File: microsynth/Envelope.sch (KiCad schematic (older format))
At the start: 42 parts, among them Q3 BC548, SW18-ENV-TO-VCF1 SW_SPDT, SW19-ENV-TO-VCO1 SW_SPDT, SW20-ENV-TO-KEYB1 SW_SPDT, SW7 SW_SPDT, SW8 SUSTAIN, SW9 TRIGGER, U10 LM741, U3 4011, U4 4016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

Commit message: Clean up repo
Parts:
- U5: symbol Amplifier_Operational:LF347 -> microsynth-rescue:LF347-Amplifier_Operational
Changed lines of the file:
@@
 $EndComp
 $Comp
-L Amplifier_Operational:LF347 U?
+L microsynth-rescue:LF347-Amplifier_Operational U?
 U 2 1 5E8FB113
 P 10250 3650
 AR Path="/5E8C1704/5E8FB113" Ref="U?"  Part="2"
 AR Path="/5E5B9865/5E8FB113" Ref="U5"  Part="2"
+AR Path="/5E8FB113" Ref="U5"  Part="2"
 F 0 "U5" H 10250 4050 50  0000 C CNN
 F 1 "LF347" H 10250 3950 50  0000 C CNN

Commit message: Replace dodgy parts 1458, 4136 & LF351s
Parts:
- removed U5: LF347, Package_DIP:DIP-14_W7.62mm_LongPads, symbol microsynth-rescue:LF347-Amplifier_Operational
- added U5: LF347, Package_DIP:DIP-14_W7.62mm_LongPads, symbol pe_microsynth:LF347
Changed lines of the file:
@@
-$EndComp
-$Comp
-L microsynth-rescue:LF347-Amplifier_Operational U?
-U 2 1 5E8FB113
-P 10250 3650
-AR Path="/5E8C1704/5E8FB113" Ref="U?"  Part="2"
-AR Path="/5E5B9865/5E8FB113" Ref="U5"  Part="2"
-AR Path="/5E8FB113" Ref="U5"  Part="2"
-F 0 "U5" H 10250 4050 50  0000 C CNN
-F 1 "LF347" H 10250 3950 50  0000 C CNN
-F 2 "Package_DIP:DIP-14_W7.62mm_LongPads" H 10200 3750 50  0001 C CNN
-F 3 "https://www.ti.com/lit/ds/symlink/lf147.pdf" H 10300 3850 50  0001 C CNN
-	2    10250 3650
-	1    0    0    -1
 $EndComp
 $Comp
@@
 	1    0    0    1
 $EndComp
+$Comp
+L pe_microsynth:LF347 U?
+U 2 1 5EBDD19A
+P 10250 3650
+AR Path="/5E8C1704/5EBDD19A" Ref="U?"  Part="2"
+AR Path="/5E5B9865/5EBDD19A" Ref="U5"  Part="2"
+F 0 "U5" H 10250 4050 50  0000 C CNN
+F 1 "LF347" H 10250 3950 50  0000 C CNN
+F 2 "Package_DIP:DIP-14_W7.62mm_LongPads" H 10200 3750 50  0001 C CNN
+F 3 "https://www.bitsbox.co.uk/data/analog/LF347.pdf" H 10300 3850 50  0001 C CNN
+	2    10250 3650
+	1    0    0    -1
+$EndComp
 $EndSCHEMATC

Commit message: Replace DP3T footprint, proper wire pads
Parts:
- SW8: symbol Switch:SW_DPTT_SELECTOR-Switch -> pe_microsynth:SW_DPTT_SELECTOR-Switch
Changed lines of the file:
@@
 $EndComp
 $Comp
-L Switch:SW_DPTT_SELECTOR-Switch SW8
+L pe_microsynth:SW_DPTT_SELECTOR-Switch SW8
 U 2 1 5F2DFAB2
 P 2950 3550
+AR Path="/5F2DFAB2" Ref="SW8"  Part="2"
+AR Path="/5E5B9865/5F2DFAB2" Ref="SW8"  Part="2"
 F 0 "SW8" H 3200 3750 50  0000 L CNN
 F 1 "SUSTAIN" H 3200 3650 50  0000 L CNN
@@
 $EndComp
 $Comp
-L Switch:SW_DPTT_SELECTOR-Switch SW8
+L pe_microsynth:SW_DPTT_SELECTOR-Switch SW8
 U 1 1 5F2DEA06
 P 2950 3650
+AR Path="/5F2DEA06" Ref="SW8"  Part="1"
+AR Path="/5E5B9865/5F2DEA06" Ref="SW8"  Part="1"
 F 0 "SW8" H 3200 3650 50  0000 L CNN
 F 1 "SUSTAIN" H 3200 3550 50  0000 L CNN

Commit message: Consolidate switches
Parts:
- added R154: 100k, Resistor_THT:R_Axial_DIN0207_L6.3mm_D2.5mm_P10.16mm_Horizontal, symbol Device:R
- SW18: renamed from SW18-ENV-TO-VCF1; footprint Buttons_Switches_ThroughHole:GF-624-6014 -> microsynth:11-SS-22-701C; Label (none) -> ENV-TO-VCF1
- SW19: renamed from SW19-ENV-TO-VCO1; footprint Buttons_Switches_ThroughHole:GF-624-6014 -> microsynth:11-SS-22-701C; Label (none) -> ENV-TO-VCO1
- SW20: renamed from SW20-ENV-TO-KEYB1; footprint Buttons_Switches_ThroughHole:GF-624-6014 -> microsynth:11-SS-22-701C; Label (none) -> ENV-TO-KEYB1
- SW7: footprint Buttons_Switches_ThroughHole:GF-624-6014 -> microsynth:11-SS-22-701C
- SW8: value SUSTAIN -> SW_DP3T; footprint Buttons_Switches_ThroughHole:G-1128S-1110 -> microsynth:11-SS-23-832C; Label (none) -> SUSTAIN
- SW8: value SUSTAIN -> SW_DP3T; footprint Buttons_Switches_ThroughHole:G-1128S-1110 -> microsynth:11-SS-23-832C; Label Sustain -> SUSTAIN
- SW9: value TRIGGER -> SW_DP3T; footprint Buttons_Switches_ThroughHole:G-1128S-1110 -> microsynth:11-SS-23-832C; Label (none) -> TRIGGER
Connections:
- wire segments 194 -> 195
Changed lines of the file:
@@
 	4350 3050 3850 3050
 Wire Wire Line
-	3850 3050 3850 3300
+	3850 3050 3850 3200
 $Comp
 L power:+VSW #PWR?
@@
 Connection ~ 2200 3900
 Wire Wire Line
-	3000 3350 3000 3300
-Wire Wire Line
-	3000 3300 3850 3300
-Connection ~ 3850 3300
-Wire Wire Line
 	3100 3350 3500 3350
 Wire Wire Line
@@
 F 0 "SW7" V 3859 1712 50  0000 R CNN
 F 1 "SW_SPDT" V 3950 1712 50  0000 R CNN
-F 2 "Buttons_Switches_ThroughHole:GF-624-6014" H 3950 1900 50  0001 C CNN
+F 2 "microsynth:11-SS-22-701C" H 3950 1900 50  0001 C CNN
 F 3 "~" H 3950 1900 50  0001 C CNN
 F 4 "ADSR" V 4041 1712 50  0000 R CNN "Label"
@@
 	7400 2600 7600 2600
 $Comp
-L Switch:SW_SPDT SW19-ENV-TO-VCO1
+L Switch:SW_SPDT SW19
 U 1 1 5E85AAE1
 P 7750 1700
-F 0 "SW19-ENV-TO-VCO1" H 7750 1985 50  0000 C CNN
+F 0 "SW19" H 7750 1985 50  0000 C CNN
 F 1 "SW_SPDT" H 7750 1894 50  0000 C CNN
-F 2 "Buttons_Switches_ThroughHole:GF-624-6014" H 7750 1700 50  0001 C CNN
+F 2 "microsynth:11-SS-22-701C" H 7750 1700 50  0001 C CNN
 F 3 "~" H 7750 1700 50  0001 C CNN
+F 4 "ENV-TO-VCO1" H 8200 1950 50  0000 C CNN "Label"
 	1    7750 1700
 	1    0    0    -1
@@
 	7400 1700 7400 2400
 $Comp
-L Switch:SW_SPDT SW18-ENV-TO-VCF1
+L Switch:SW_SPDT SW18
 U 1 1 5E881667
 P 7750 2400
-F 0 "SW18-ENV-TO-VCF1" H 7750 2685 50  0000 C CNN
+F 0 "SW18" H 7750 2685 50  0000 C CNN
 F 1 "SW_SPDT" H 7750 2594 50  0000 C CNN
-F 2 "Buttons_Switches_ThroughHole:GF-624-6014" H 7750 2400 50  0001 C CNN
+F 2 "microsynth:11-SS-22-701C" H 7750 2400 50  0001 C CNN
 F 3 "~" H 7750 2400 50  0001 C CNN
+F 4 "ENV-TO-VCF1" H 8200 2650 50  0000 C CNN "Label"
 	1    7750 2400
 	1    0    0    -1
@@
 P 7700 4800
 F 0 "SW9" H 7900 4800 50  0000 L CNN
-F 1 "TRIGGER" H 7900 4700 50  0000 L CNN
-F 2 "Buttons_Switches_ThroughHole:G-1128S-1110" H 7700 4800 50  0001 C CNN
+F 1 "SW_DP3T" H 7900 4700 50  0000 L CNN
+F 2 "microsynth:11-SS-23-832C" H 7700 4800 50  0001 C CNN
 F 3 "" H 7700 4800 50  0001 C CNN
+F 4 "TRIGGER" H 7700 4800 50  0001 C CNN "Label"
 	2    7700 4800
 	-1   0    0    1
 $EndComp
 $Comp
-L Switch:SW_SPDT SW20-ENV-TO-KEYB1
+L Switch:SW_SPDT SW20
 U 1 1 5E83D5A9
 P 7750 1000
-F 0 "SW20-ENV-TO-KEYB1" H 7750 1285 50  0000 C CNN
+F 0 "SW20" H 7750 1285 50  0000 C CNN
 F 1 "SW_SPDT" H 7750 1194 50  0000 C CNN
-F 2 "Buttons_Switches_ThroughHole:GF-624-6014" H 7750 1000 50  0001 C CNN
+F 2 "microsynth:11-SS-22-701C" H 7750 1000 50  0001 C CNN
 F 3 "~" H 7750 1000 50  0001 C CNN
+F 4 "ENV-TO-KEYB1" H 8200 1250 50  0000 C CNN "Label"
 	1    7750 1000
 	1    0    0    -1
@@
 AR Path="/5E5B9865/5F2DFAB2" Ref="SW8"  Part="2"
 F 0 "SW8" H 3200 3750 50  0000 L CNN
-F 1 "SUSTAIN" H 3200 3650 50  0000 L CNN
-F 2 "Buttons_Switches_ThroughHole:G-1128S-1110" H 2950 3550 50  0001 C CNN
+F 1 "SW_DP3T" H 3200 3650 50  0000 L CNN
+F 2 "microsynth:11-SS-23-832C" H 2950 3550 50  0001 C CNN
 F 3 "http://switches-connectors-custom.cwind.com/Asset/G-1128S-1110_2D%20DRAWING.pdf" H 2950 3550 50  0001 C CNN
-F 4 "Sustain" H 3200 3550 50  0001 L CNN "Label"
+F 4 "SUSTAIN" H 3200 3550 50  0001 L CNN "Label"
 	2    2950 3550
 	1    0    0    -1
@@
 AR Path="/5E5B9865/5F2DEA06" Ref="SW8"  Part="1"
 F 0 "SW8" H 3200 3650 50  0000 L CNN
-F 1 "SUSTAIN" H 3200 3550 50  0000 L CNN
-F 2 "Buttons_Switches_ThroughHole:G-1128S-1110" H 2950 3650 50  0001 C CNN
+F 1 "SW_DP3T" H 3200 3550 50  0000 L CNN
+F 2 "microsynth:11-SS-23-832C" H 2950 3650 50  0001 C CNN
 F 3 "http://switches-connectors-custom.cwind.com/Asset/G-1128S-1110_2D%20DRAWING.pdf" H 2950 3650 50  0001 C CNN
+F 4 "SUSTAIN" H 3350 3750 50  0000 C CNN "Label"
 	1    2950 3650
 	1    0    0    -1
@@
 Wire Wire Line
 	3400 3800 4050 3800
-Wire Wire Line
-	3850 3300 3850 3950
 $Comp
 L Device:D D5
@@
 	1    0    0    -1
 $EndComp
+Wire Wire Line
+	3000 3200 3100 3200
+Wire Wire Line
+	3400 3200 3850 3200
+Connection ~ 3850 3200
+Wire Wire Line
+	3000 3200 3000 3350
+Wire Wire Line
+	3850 3200 3850 3950
+$Comp
+L Device:R R154
+U 1 1 5ED83FC1
+P 3250 3200
+F 0 "R154" V 3043 3200 50  0000 C CNN
+F 1 "100k" V 3134 3200 50  0000 C CNN
+F 2 "Resistor_THT:R_Axial_DIN0207_L6.3mm_D2.5mm_P10.16mm_Horizontal" V 3180 3200 50  0001 C CNN
+F 3 "~" H 3250 3200 50  0001 C CNN
+	1    3250 3200
+	0    1    1    0
+$EndComp
 $EndSCHEMATC

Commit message: Consolidate all(?) switches
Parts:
- RV10, RV12, RV9: footprint 4ms_Potentiometer:Pot_16mm_NoDet_RV16AF-4A -> microsynth:Pot_16mm_NoDet_RV16AF-4A
- SW9: symbol microsynth-rescue:SW_DPTT_SELECTOR-Switch -> pe_microsynth:SW_DPTT_SELECTOR-Switch
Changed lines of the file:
@@
 F 0 "RV10" H 4280 4946 50  0000 R CNN
 F 1 "2MLOG" H 4280 4855 50  0000 R CNN
-F 2 "4ms_Potentiometer:Pot_16mm_NoDet_RV16AF-4A" H 4350 4900 50  0001 C CNN
+F 2 "microsynth:Pot_16mm_NoDet_RV16AF-4A" H 4350 4900 50  0001 C CNN
 F 3 "~" H 4350 4900 50  0001 C CNN
 F 4 "Release" H 4100 4750 50  0000 C BNN "Label"
@@
 F 0 "RV9" H 4280 3346 50  0000 R CNN
 F 1 "1MLOG" H 4280 3255 50  0000 R CNN
-F 2 "4ms_Potentiometer:Pot_16mm_NoDet_RV16AF-4A" H 4350 3300 50  0001 C CNN
+F 2 "microsynth:Pot_16mm_NoDet_RV16AF-4A" H 4350 3300 50  0001 C CNN
 F 3 "~" H 4350 3300 50  0001 C CNN
 F 4 "Attack" H 4150 3150 50  0000 C CNN "Label"
@@
 F 0 "RV12" H 6580 3596 50  0000 R CNN
 F 1 "100kLIN" H 6580 3505 50  0000 R CNN
-F 2 "4ms_Potentiometer:Pot_16mm_NoDet_RV16AF-4A" H 6650 3550 50  0001 C CNN
+F 2 "microsynth:Pot_16mm_NoDet_RV16AF-4A" H 6650 3550 50  0001 C CNN
 F 3 "~" H 6650 3550 50  0001 C CNN
 F 4 "Env Level" H 6550 3450 50  0000 R TNN "Label"
@@
 	5150 4450 5150 5150
 $Comp
-L microsynth-rescue:SW_DPTT_SELECTOR-Switch SW9
+L pe_microsynth:SW_DPTT_SELECTOR-Switch SW9
 U 2 1 5E95BE3D
 P 7700 4800

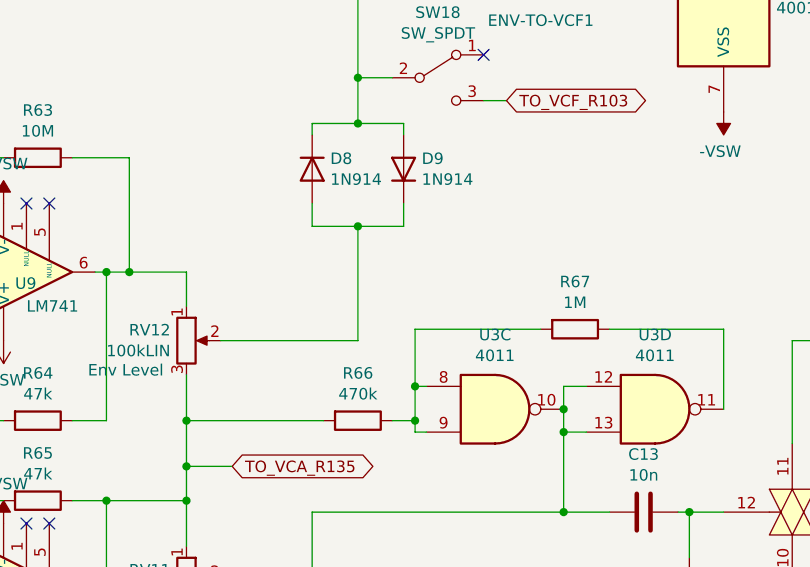
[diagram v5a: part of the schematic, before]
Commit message: Add test points
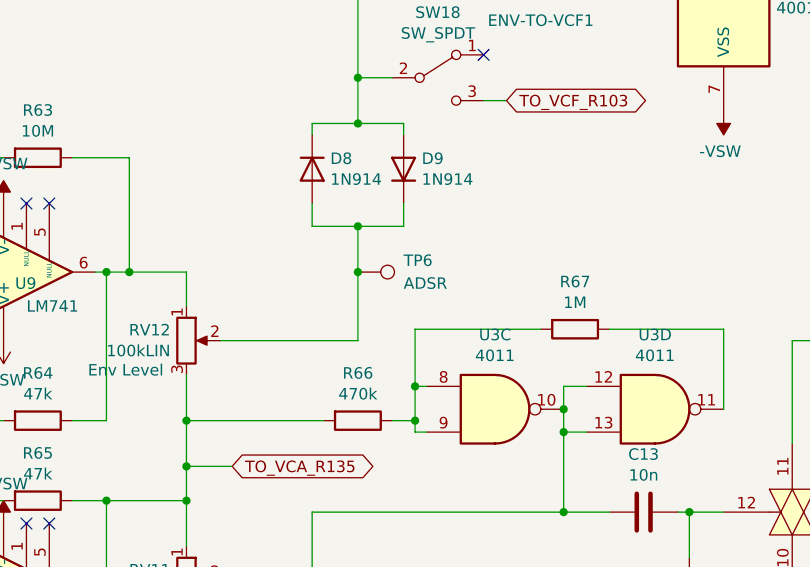
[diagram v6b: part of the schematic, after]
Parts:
- added TP6: ADSR, TestPoint:TestPoint_Pad_D2.0mm, symbol Connector:TestPoint
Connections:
- net at D8.2 (A), D9.1 (K), RV12.2: now also TP6.1
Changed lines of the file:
@@
 	7200 3050 7200 2950
 Wire Wire Line
-	7400 3050 7400 3550
+	7400 3050 7400 3250
 Wire Wire Line
 	7400 3550 6800 3550
@@
 	0    1    1    0
 $EndComp
+$Comp
+L Connector:TestPoint TP?
+U 1 1 5EE196DB
+P 7400 3250
+AR Path="/5E475532/5EE196DB" Ref="TP?"  Part="1"
+AR Path="/5E5B9865/5EE196DB" Ref="TP6"  Part="1"
+F 0 "TP6" V 7350 3450 50  0000 L CNN
+F 1 "ADSR" V 7450 3450 50  0000 L CNN
+F 2 "TestPoint:TestPoint_Pad_D2.0mm" H 7600 3250 50  0001 C CNN
+F 3 "~" H 7600 3250 50  0001 C CNN
+	1    7400 3250
+	0    1    1    0
+$EndComp
+Connection ~ 7400 3250
+Wire Wire Line
+	7400 3250 7400 3550
 $EndSCHEMATC

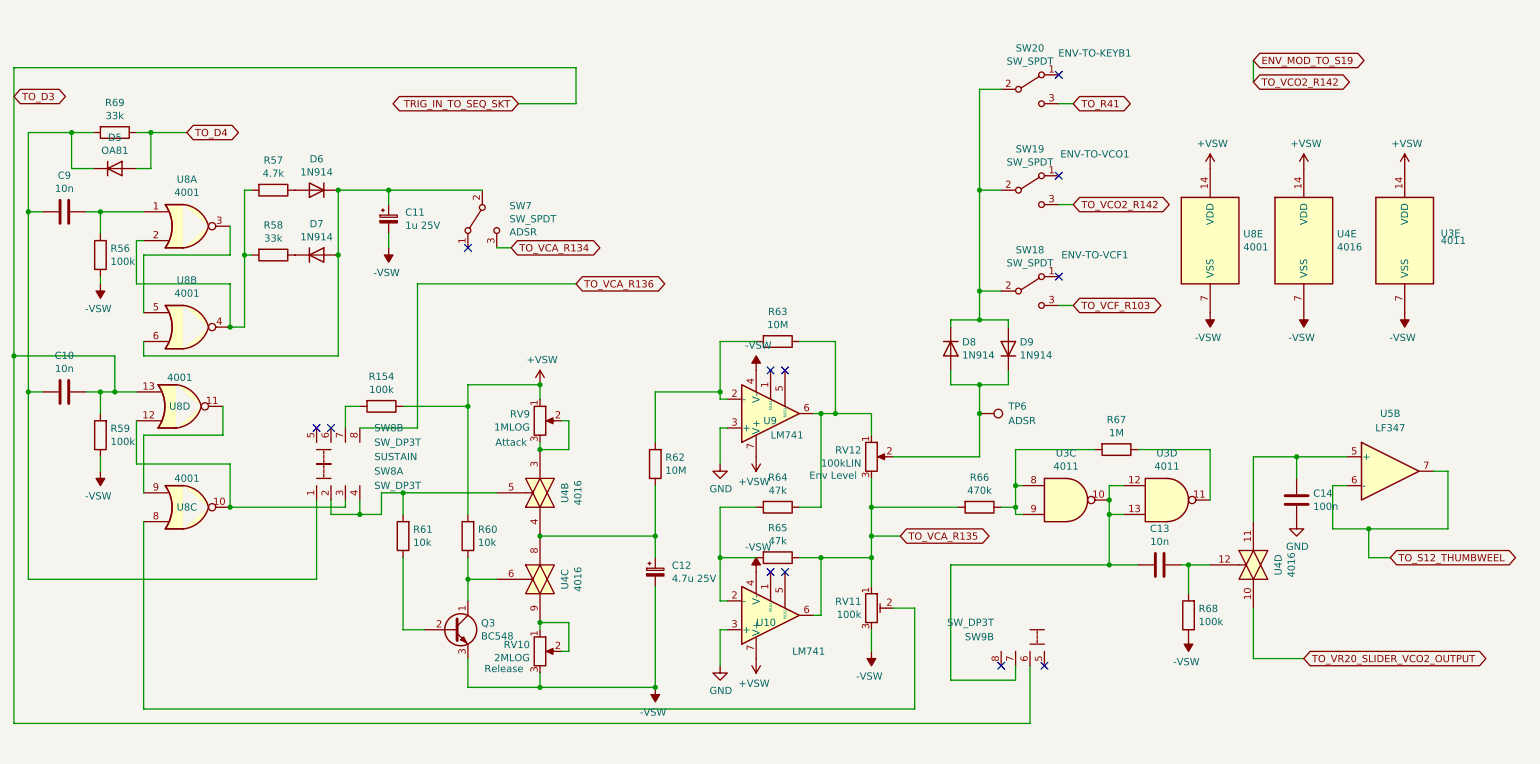
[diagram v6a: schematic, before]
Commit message: Replace IC1 with LM348, update component values
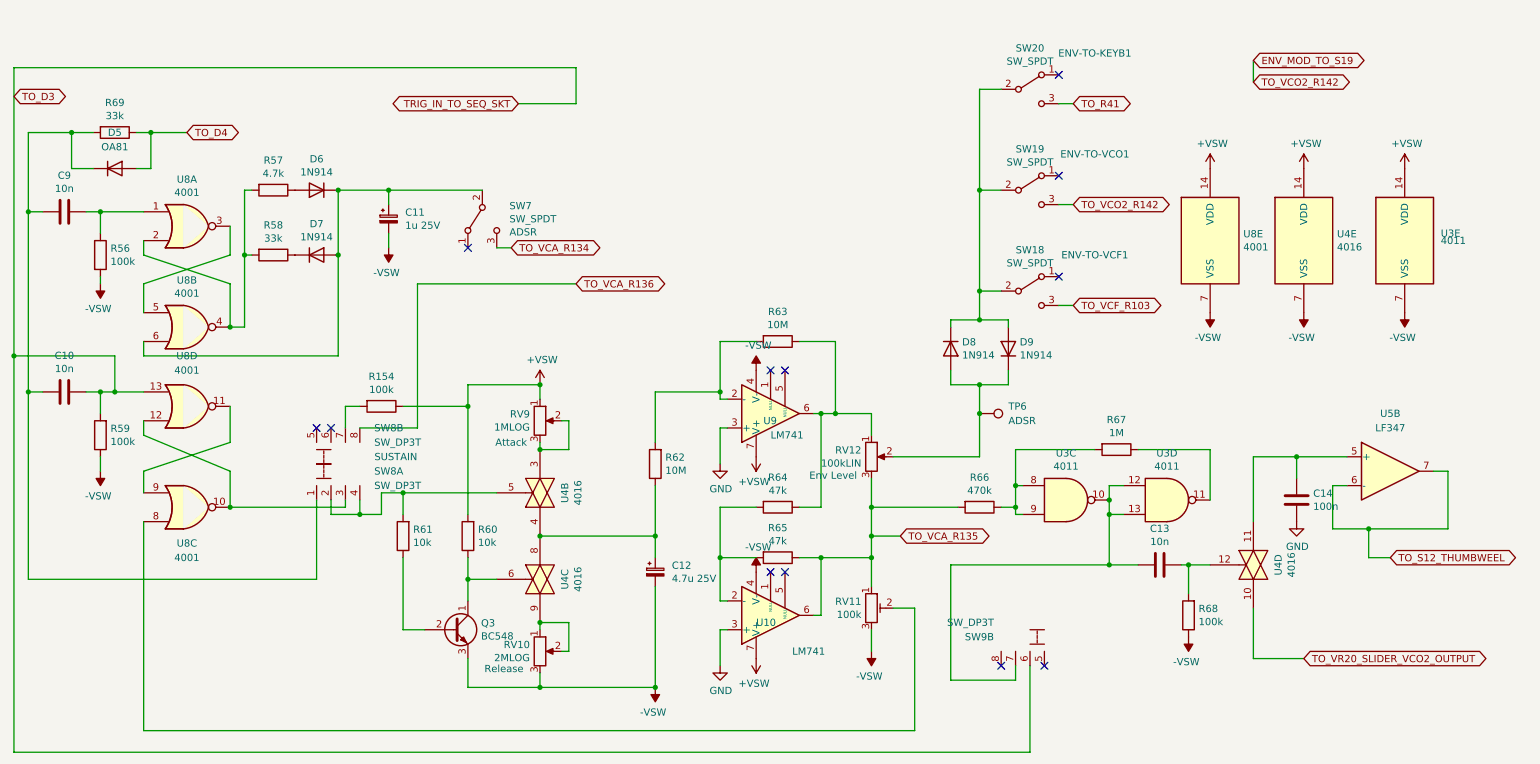
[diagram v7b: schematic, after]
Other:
- moved on the sheet: U8D
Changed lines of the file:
@@
 U 3 1 5E5BF1E4
 P 1900 3900
-F 0 "U8" H 1900 3900 50  0000 C CNN
-F 1 "4001" H 1900 3700 50  0000 C CNN
+F 0 "U8" H 1900 4150 50  0000 C CNN
+F 1 "4001" H 1900 4250 50  0000 C CNN
 F 2 "Package_DIP:DIP-14_W7.62mm_LongPads" H 1900 3900 50  0001 C CNN
 F 3 "http://www.intersil.com/content/dam/Intersil/documents/cd40/cd4000bms-01bms-02bms-25bms.pdf" H 1900 3900 50  0001 C CNN
@@
 L 4xxx:4001 U8
 U 4 1 5E5BFBC6
-P 1850 3200
-F 0 "U8" H 1850 3200 50  0000 C CNN
-F 1 "4001" H 1850 3000 50  0000 C CNN
-F 2 "Package_DIP:DIP-14_W7.62mm_LongPads" H 1850 3200 50  0001 C CNN
-F 3 "http://www.intersil.com/content/dam/Intersil/documents/cd40/cd4000bms-01bms-02bms-25bms.pdf" H 1850 3200 50  0001 C CNN
-	4    1850 3200
+P 1900 3200
+F 0 "U8" H 1900 2850 50  0000 C CNN
+F 1 "4001" H 1900 2950 50  0000 C CNN
+F 2 "Package_DIP:DIP-14_W7.62mm_LongPads" H 1900 3200 50  0001 C CNN
+F 3 "http://www.intersil.com/content/dam/Intersil/documents/cd40/cd4000bms-01bms-02bms-25bms.pdf" H 1900 3200 50  0001 C CNN
+	4    1900 3200
 	1    0    0    1
 $EndComp
@@
 $EndComp
 Wire Wire Line
-	2200 3900 2200 3600
-Wire Wire Line
-	2200 3600 1550 3600
-Wire Wire Line
-	1550 3600 1550 3300
-Wire Wire Line
-	1600 3800 1600 3400
-Wire Wire Line
-	1600 3400 2150 3400
-Wire Wire Line
-	2150 3400 2150 3200
-Wire Wire Line
-	1600 2150 2200 2150
+	1600 3800 1600 3650
 Wire Wire Line
 	2200 2150 2200 1950
 Wire Wire Line
-	1600 2550 1600 2150
-Wire Wire Line
-	1600 2050 1550 2050
-Wire Wire Line
-	1550 2050 1550 2350
-Wire Wire Line
-	1550 2350 2200 2350
+	1600 2550 1600 2350
 Wire Wire Line
 	2200 2350 2200 2650
@@
 	6800 4600 6950 4600
 Wire Wire Line
-	6950 4600 6950 5300
-Wire Wire Line
-	6950 5300 1600 5300
-Wire Wire Line
-	1600 5300 1600 4000
+	6950 4600 6950 5450
+Wire Wire Line
+	6950 5450 1600 5450
+Wire Wire Line
+	1600 5450 1600 4000
 Wire Wire Line
 	2800 3850 2800 4400
@@
 Wire Wire Line
 	3000 3900 3000 3850
-Connection ~ 2200 3900
 Wire Wire Line
 	3100 3350 3500 3350
@@
 Connection ~ 1400 3100
 Wire Wire Line
-	1400 3100 1550 3100
-Wire Wire Line
-	700  5400 700  2850
+	1400 3100 1600 3100
+Wire Wire Line
+	700  5600 700  2850
 Connection ~ 700  2850
 Wire Wire Line
@@
 NoConn ~ 7850 5000
 Wire Wire Line
-	7750 5000 7750 5400
-Wire Wire Line
-	7750 5400 700  5400
+	7750 5000 7750 5600
+Wire Wire Line
+	7750 5600 700  5600
 Wire Wire Line
 	8500 4300 8300 4300
@@
 U 1 1 5E6BA831
 P 1400 1550
-F 0 "D5" H 1400 1766 50  0000 C CNN
-F 1 "OA81" H 1400 1675 50  0000 C CNN
+F 0 "D5" H 1400 1800 50  0000 C CNN
+F 1 "OA81" H 1400 1700 50  0000 C CNN
 F 2 "Diode_THT:D_A-405_P10.16mm_Horizontal" H 1400 1550 50  0001 C CNN
 F 3 "~" H 1400 1550 50  0001 C CNN
@@
 Wire Wire Line
 	7400 3250 7400 3550
+Wire Wire Line
+	2200 2150 1600 2350
+Wire Wire Line
+	1600 2050 1600 2150
+Wire Wire Line
+	1600 2150 2200 2350
+Wire Wire Line
+	1600 3650 2200 3450
+Wire Wire Line
+	2200 3200 2200 3450
+Connection ~ 2200 3900
+Wire Wire Line
+	2200 3900 2200 3650
+Wire Wire Line
+	2200 3650 1600 3400
+Wire Wire Line
+	1600 3400 1600 3300
 $EndSCHEMATC

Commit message: Annotate schematic
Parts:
- SW19: Label ENV-TO-VCO1 -> ENV-TO-VCO2
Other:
- note added: "ADSR"
- note added: "ENVELOPE MOD"
- note added: "KBD"
- note added: "KBD RPT LFO"
- note added: "MAN. AUTO HOLD"
- note added: "ON"
- note added: "SUSTAIN"
- note added: "TRIGGER"
- note added: "VCF"
- note added: "VCO2"
- moved on the sheet: R154
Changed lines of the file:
@@
 Wire Wire Line
 	4350 3050 3850 3050
-Wire Wire Line
-	3850 3050 3850 3200
 $Comp
 L power:+VSW #PWR?
@@
 	3000 3900 3000 3850
 Wire Wire Line
-	3100 3350 3500 3350
-Wire Wire Line
-	3500 3350 3500 2350
-Wire Wire Line
-	3500 2350 4600 2350
+	3100 2350 4600 2350
 $Comp
 L Transistor_BJT:BC548 Q3
@@
 F 2 "microsynth:11-SS-22-701C" H 7750 1700 50  0001 C CNN
 F 3 "~" H 7750 1700 50  0001 C CNN
-F 4 "ENV-TO-VCO1" H 8200 1950 50  0000 C CNN "Label"
+F 4 "ENV-TO-VCO2" H 8200 1950 50  0000 C CNN "Label"
 	1    7750 1700
 	1    0    0    -1
@@
 $EndComp
 Wire Wire Line
-	3000 3200 3100 3200
-Wire Wire Line
-	3400 3200 3850 3200
-Connection ~ 3850 3200
-Wire Wire Line
 	3000 3200 3000 3350
-Wire Wire Line
-	3850 3200 3850 3950
-$Comp
-L Device:R R154
-U 1 1 5ED83FC1
-P 3250 3200
-F 0 "R154" V 3043 3200 50  0000 C CNN
-F 1 "100k" V 3134 3200 50  0000 C CNN
-F 2 "Resistor_THT:R_Axial_DIN0207_L6.3mm_D2.5mm_P10.16mm_Horizontal" V 3180 3200 50  0001 C CNN
-F 3 "~" H 3250 3200 50  0001 C CNN
-	1    3250 3200
-	0    1    1    0
-$EndComp
 $Comp
 L Connector:TestPoint TP?
@@
 Wire Wire Line
 	1600 3400 1600 3300
+Text Notes 3950 1500 0    50   ~ 0
+ADSR
+Text Notes 4050 1650 0    50   ~ 0
+ON
+Text Notes 2800 2950 0    50   ~ 0
+SUSTAIN
+Text Notes 2700 3100 0    50   ~ 0
+MAN. AUTO HOLD
+Wire Wire Line
+	3100 3350 3100 2350
+Wire Wire Line
+	3000 3200 3350 3200
+Wire Wire Line
+	3850 3200 3850 3950
+$Comp
+L Device:R R154
+U 1 1 5ED83FC1
+P 3500 3200
+F 0 "R154" V 3293 3200 50  0000 C CNN
+F 1 "100k" V 3384 3200 50  0000 C CNN
+F 2 "Resistor_THT:R_Axial_DIN0207_L6.3mm_D2.5mm_P10.16mm_Horizontal" V 3430 3200 50  0001 C CNN
+F 3 "~" H 3500 3200 50  0001 C CNN
+	1    3500 3200
+	0    1    1    0
+$EndComp
+Wire Wire Line
+	3650 3200 3850 3200
+Wire Wire Line
+	3850 3200 3850 3050
+Connection ~ 3850 3200
+Text Notes 7550 550  0    50   ~ 0
+ENVELOPE MOD
+Text Notes 8150 1000 0    50   ~ 0
+KBD
+Text Notes 8150 1700 0    50   ~ 0
+VCO2
+Text Notes 8150 2400 0    50   ~ 0
+VCF
+Text Notes 7450 4600 0    50   ~ 0
+KBD RPT LFO
+Text Notes 7900 5200 0    50   ~ 0
+TRIGGER
 $EndSCHEMATC
